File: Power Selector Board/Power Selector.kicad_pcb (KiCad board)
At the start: 2 copper layers, 23 parts, among them J101 MSD-DB01M-12P, J102 MSD-DB01F-12P_1, J103 64900221122, J104 64900221122, J105 64900221122, K101 G6SK-2G DC24, K102 J115F11C24VDCSH.9, K103 J115F11C24VDCSH.9, U101 1720466, U102 LMW78_24-0.3RL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

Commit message: Debut routing
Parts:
- removed K102, K103: J115F11C24VDCSH.9, Relays:RELAY5_J115F11C24VDCSH.9_CRS
- added H1: Mounting-Hole-M3, Connectors:Mounting_Hole_3mm, F.Cu at (58.2, 81.8)
- added H2: Mounting-Hole-M3, Connectors:Mounting_Hole_3mm, F.Cu at (58.2, 87.8)
- added H3: Mounting-Hole-M3, Connectors:Mounting_Hole_3mm, F.Cu at (58.2, 93.8)
- added H4: Mounting-Hole-M3, Connectors:Mounting_Hole_3mm, F.Cu at (58.2, 99.8)
- added RL101: RELAY8_SMTGUL_TEC, Relays:2-1462039-9, F.Cu at (166.8, 82.8)
- J101, J102: footprint Connectors:649012227222 -> Connectors:MSD-DB01F-12P-V2.0
- moved J101 107.0 mm to (206.0, 77.0), turned to -90 degrees
- moved F102 98.2 mm to (192.1, 82.6)
- moved F103 82.5 mm to (81.8, 83.7)
- moved J104 58.8 mm to (100.2, 67.3)
- moved J103 58.5 mm to (93.8, 67.5)
- moved F101 57.6 mm to (149.0, 119.4), turned to 180 degrees
- moved D101 55.4 mm to (129.3, 67.4)
- moved D102 55.4 mm to (129.3, 71.7)
- moved D103 55.4 mm to (129.3, 76.1)
- moved U101 50.3 mm to (145.2, 127.1)
- moved R101 49.5 mm to (112.8, 125.8), turned to 180 degrees
- moved J105 48.2 mm to (108.4, 130.8), turned to -90 degrees
- moved U102 43.3 mm to (96.4, 86.9), turned to 90 degrees
- moved C103 34.9 mm to (142.8, 107.0), turned to 90 degrees
- moved C102 34.4 mm to (142.8, 97.7), turned to -90 degrees
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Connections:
- C103 pad 2: 24V_Bat -> 24V
- C104 pad 2: 24V_Tether -> 24V
- F101 pad 1: +V_Drone -> (no net)
- F101 pad 2: Net-(F101-Pad2) -> (no net)
- F102 pad 1: +V_Bat -> (no net)
- F102 pad 2: Net-(F102-Pad2) -> (no net)
- F103 pad 1: +V_Bat -> +VBat
- F104 pad 1: +V_Drone -> +VBat
- J101 pad 1: +V_Drone -> Net-(F102-Pad~)
- J101 pad 2: +V_Drone -> Net-(F102-Pad~)
- J101 pad 3: +V_Drone -> Net-(F102-Pad~)
- J101 pad 4: +V_Drone -> Net-(F102-Pad~)
- J101 pad 5: +V_Drone -> Net-(F102-Pad~)
- J102 pad 1: Net-(F102-Pad2) -> +VBat
- J102 pad 2: Net-(F102-Pad2) -> +VBat
- J102 pad 3: Net-(F102-Pad2) -> +VBat
- J102 pad 4: Net-(F102-Pad2) -> +VBat
- J102 pad 5: Net-(F102-Pad2) -> +VBat
- J103 pad 1: 24V_Tether -> 24V
- J103 pad 2: Net-(D103-Pad1) -> Net-(J103-Pad2)
- J104 pad 1: Net-(J104-Pad1) -> GND
- J104 pad 2: GND -> Net-(J104-Pad2)
- J105 pad 1: 24V_Bat -> 24V
- K101 pad 1: Net-(D103-Pad1) -> GND
- K101 pad 12: GND -> Net-(J103-Pad2)
- K101 pad 6: 24V_Bat -> 24V
- K101 pad 8: 24V_Tether -> 24V
- K101 pad 9: /Relay_Active -> Net-(K101-Pad9)
- U101 pad 1: Net-(F101-Pad2) -> Net-(F101-Pad~)
- U101 pad 2: Net-(F101-Pad2) -> Net-(F101-Pad~)
- U101 pad 3: Net-(F101-Pad2) -> Net-(F101-Pad~)
- U102 pad 3: 24V_Bat -> 24V
- U103 pad 3: 24V_Tether -> 24V
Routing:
- net 24V: track 0.00 -> 62.9 mm
- net +VBat: track 0.00 -> 37.3 mm
- net Net-(U102-Vin): track 0.00 -> 14.5 mm
- net Net-(U103-Vin): track 0.00 -> 13.2 mm
- net Net-(J105-Pad2): track 0.00 -> 5.62 mm
- net (no net): track 0.00 -> 4.20 mm
- added copper zone on F.Cu, net +VBat
- added copper zone on B.Cu, net GND
- added copper zone on F.Cu, net GND
- added copper zone on F.Cu, net Net-(F101-Pad~)
- added copper zone on F.Cu, net Net-(F102-Pad~)
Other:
- board text added: "DOIT ETRE PLACÉ AU CENTRE EN X ET EN BAS EN Y POUR AVOIR UN FIT IDENTIQUE DE CHAQUE CÔTÉ DU DRONE"

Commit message: Fix du bug github, devrait etre la bonne version
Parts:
- removed H1, H2, H3, H4: Mounting-Hole-M3, Connectors:Mounting_Hole_3mm
- removed RL101: RELAY8_SMTGUL_TEC, Relays:2-1462039-9
- added K102: J115F11C24VDCSH.9, Relays:RELAY5_J115F11C24VDCSH.9_CRS, F.Cu at (120.1, 77.9)
- added K103: J115F11C24VDCSH.9, Relays:RELAY5_J115F11C24VDCSH.9_CRS, F.Cu at (149.8, 77.9)
- J101, J102: footprint Connectors:MSD-DB01F-12P-V2.0 -> Connectors:649012227222
- moved J101 107.0 mm to (100.1, 61.8), turned to 0 degrees
- moved F102 98.2 mm to (96.8, 106.4)
- moved F103 82.5 mm to (162.7, 99.8)
- moved J104 58.8 mm to (143.6, 107.0)
- moved J103 58.5 mm to (136.9, 107.0)
- moved F101 57.6 mm to (96.7, 95.2), turned to 0 degrees
- moved D101 55.4 mm to (182.5, 82.7)
- moved D102 55.4 mm to (182.5, 87.0)
- moved D103 55.4 mm to (182.5, 91.3)
- moved U101 50.3 mm to (119.9, 83.6)
- moved R101 49.5 mm to (159.1, 108.5), turned to 0 degrees
- moved J105 48.2 mm to (150.3, 107.0), turned to 0 degrees
- moved U102 43.3 mm to (139.6, 84.7), turned to 0 degrees
- moved C103 34.9 mm to (108.5, 101.0), turned to 0 degrees
- moved C102 34.4 mm to (108.5, 96.7), turned to 0 degrees
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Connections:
- C103 pad 2: 24V -> 24V_Bat
- C104 pad 2: 24V -> 24V_Tether
- F101 pad 1: (no net) -> +V_Drone
- F101 pad 2: (no net) -> Net-(F101-Pad2)
- F102 pad 1: (no net) -> +V_Bat
- F102 pad 2: (no net) -> Net-(F102-Pad2)
- F103 pad 1: +VBat -> +V_Bat
- F104 pad 1: +VBat -> +V_Drone
- J101 pad 1: Net-(F102-Pad~) -> +V_Drone
- J101 pad 2: Net-(F102-Pad~) -> +V_Drone
- J101 pad 3: Net-(F102-Pad~) -> +V_Drone
- J101 pad 4: Net-(F102-Pad~) -> +V_Drone
- J101 pad 5: Net-(F102-Pad~) -> +V_Drone
- J102 pad 1: +VBat -> Net-(F102-Pad2)
- J102 pad 2: +VBat -> Net-(F102-Pad2)
- J102 pad 3: +VBat -> Net-(F102-Pad2)
- J102 pad 4: +VBat -> Net-(F102-Pad2)
- J102 pad 5: +VBat -> Net-(F102-Pad2)
- J103 pad 1: 24V -> 24V_Tether
- J103 pad 2: Net-(J103-Pad2) -> Net-(D103-Pad1)
- J104 pad 1: GND -> Net-(J104-Pad1)
- J104 pad 2: Net-(J104-Pad2) -> GND
- J105 pad 1: 24V -> 24V_Bat
- K101 pad 1: GND -> Net-(D103-Pad1)
- K101 pad 12: Net-(J103-Pad2) -> GND
- K101 pad 6: 24V -> 24V_Bat
- K101 pad 8: 24V -> 24V_Tether
- K101 pad 9: Net-(K101-Pad9) -> /Relay_Active
- U101 pad 1: Net-(F101-Pad~) -> Net-(F101-Pad2)
- U101 pad 2: Net-(F101-Pad~) -> Net-(F101-Pad2)
- U101 pad 3: Net-(F101-Pad~) -> Net-(F101-Pad2)
- U102 pad 3: 24V -> 24V_Bat
- U103 pad 3: 24V -> 24V_Tether
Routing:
- net 24V: track 62.9 -> 0.00 mm
- net +VBat: track 37.3 -> 0.00 mm
- net Net-(U102-Vin): track 14.5 -> 0.00 mm
- net Net-(U103-Vin): track 13.2 -> 0.00 mm
- net Net-(J105-Pad2): track 5.62 -> 0.00 mm
- net (no net): track 4.20 -> 0.00 mm
- removed copper zone on F.Cu, net +VBat
- removed copper zone on B.Cu, net GND
- removed copper zone on F.Cu, net GND
- removed copper zone on F.Cu, net Net-(F101-Pad~)
- removed copper zone on F.Cu, net Net-(F102-Pad~)
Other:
- board text removed: "DOIT ETRE PLACÉ AU CENTRE EN X ET EN BAS EN Y POUR AVOIR UN FIT IDENTIQUE DE CHAQUE CÔTÉ DU DRONE"

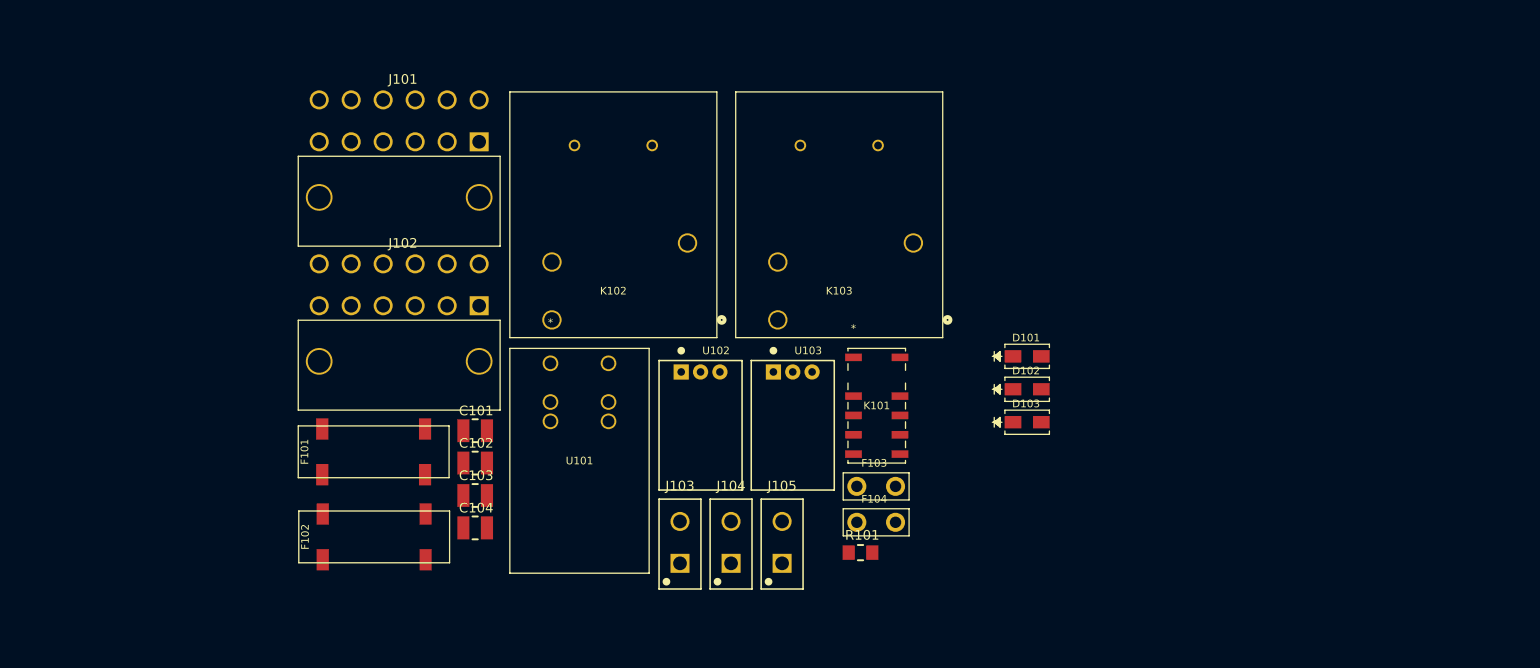
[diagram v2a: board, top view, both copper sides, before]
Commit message: Ajout des deux PCB (droit et gauche) sur le meme PCB
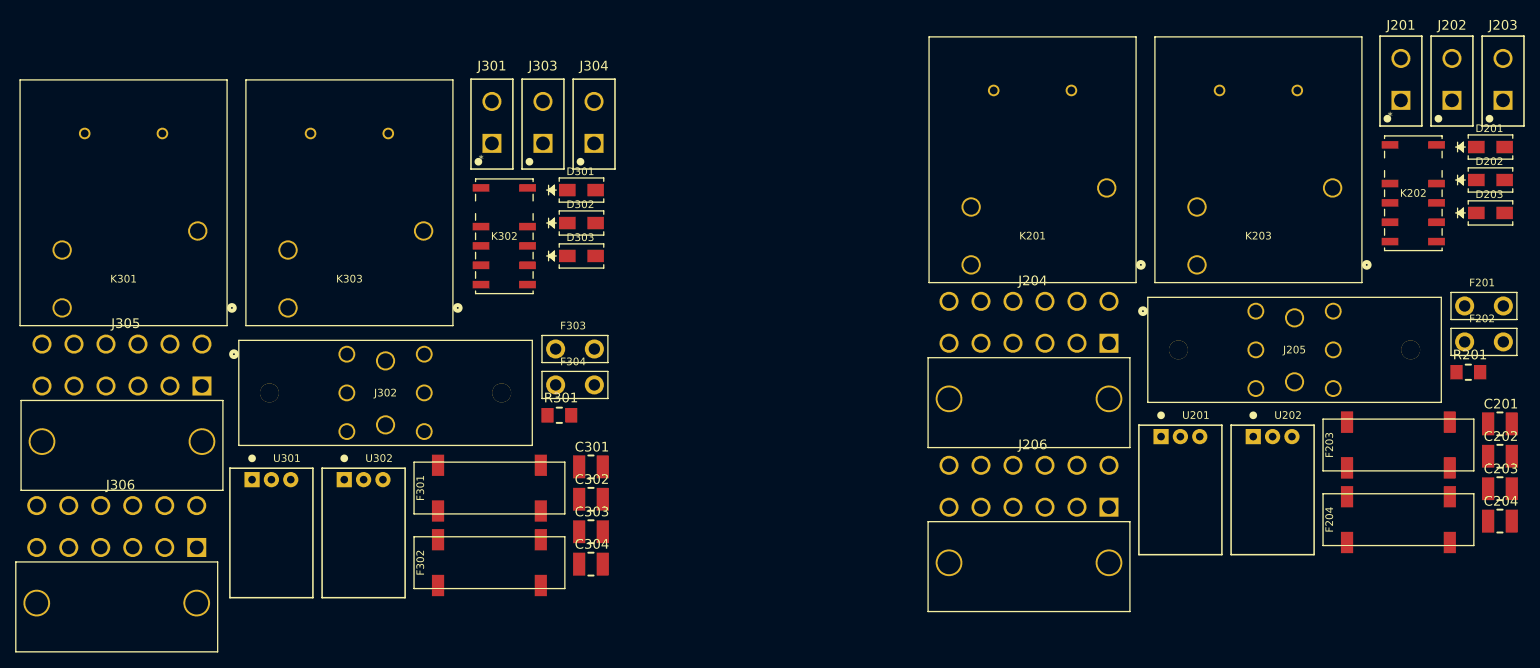
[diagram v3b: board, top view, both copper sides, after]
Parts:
- removed C101, C102, C103, C104: GRM32EC72A106ME05L, Capacitors:C1210
- removed D101, D102, D103: S1D-13-F, Diodes:SMA_DIO
- removed F101, F102: 047706.3MRET1P, Fuses:3587TR
- removed F103, F104: 0698Q2000-02, Fuses:TE5_395
- removed J101: MSD-DB01M-12P, Connectors:649012227222
- removed J102: MSD-DB01F-12P_1, Connectors:649012227222
- removed J103, J104, J105: 64900221122, Connectors:64900221122
- removed K101: G6SK-2G DC24, Relays:G6SK-2G DC3_OMR
- removed K102, K103: J115F11C24VDCSH.9, Relays:RELAY5_J115F11C24VDCSH.9_CRS
- removed R101: RC1206JR-07120RL, Resistors:R1206
- removed U101: 1720466, Connectors:1720466_PXC
- removed U102, U103: LMW78_24-0.3RL, Assembly:OKI-78SR_Horizontal
- added C201: GRM32EC72A106ME05L, Capacitors:C1210, F.Cu at (243.0, 91.6)
- added C202: GRM32EC72A106ME05L, Capacitors:C1210, F.Cu at (243.0, 95.8)
- added C203: GRM32EC72A106ME05L, Capacitors:C1210, F.Cu at (243.0, 100.1)
- added C204: GRM32EC72A106ME05L, Capacitors:C1210, F.Cu at (243.0, 104.3)
- added C301: GRM32EC72A106ME05L, Capacitors:C1210, F.Cu at (123.7, 97.2)
- added C302: GRM32EC72A106ME05L, Capacitors:C1210, F.Cu at (123.7, 101.5)
- added C303: GRM32EC72A106ME05L, Capacitors:C1210, F.Cu at (123.7, 105.7)
- added C304: GRM32EC72A106ME05L, Capacitors:C1210, F.Cu at (123.7, 110.0)
- added D201: S1D-13-F, Diodes:SMA_DIO, F.Cu at (243.3, 55.2)
- added D202: S1D-13-F, Diodes:SMA_DIO, F.Cu at (243.3, 59.5)
- added D203: S1D-13-F, Diodes:SMA_DIO, F.Cu at (243.3, 63.9)
- added D301: S1D-13-F, Diodes:SMA_DIO, F.Cu at (124.0, 60.9)
- added D302: S1D-13-F, Diodes:SMA_DIO, F.Cu at (124.0, 65.2)
- added D303: S1D-13-F, Diodes:SMA_DIO, F.Cu at (124.0, 69.5)
- added F201: 0698Q2000-02, Fuses:TE5_395, F.Cu at (242.5, 76.1)
- added F202: 0698Q2000-02, Fuses:TE5_395, F.Cu at (242.5, 80.8)
- added F203: 047706.3MRET1P, Fuses:3587TR, F.Cu at (231.2, 94.3)
- added F204: 047706.3MRET1P, Fuses:3587TR, F.Cu at (231.2, 104.1)
- added F301: 047706.3MRET1P, Fuses:3587TR, F.Cu at (111.9, 100.0)
- added F302: 047706.3MRET1P, Fuses:3587TR, F.Cu at (111.9, 109.8)
- added F303: 0698Q2000-02, Fuses:TE5_395, F.Cu at (123.1, 81.7)
- added F304: 0698Q2000-02, Fuses:TE5_395, F.Cu at (123.1, 86.4)
- added J201: 64900221122, Connectors:64900221122, F.Cu at (231.6, 46.2)
- added J202: 64900221122, Connectors:64900221122, F.Cu at (238.3, 46.2)
- added J203: 64900221122, Connectors:64900221122, F.Cu at (245.0, 46.2)
- added J204: MSD-DB01M-12P, Connectors:649012227222, F.Cu at (182.7, 88.3)
- added J205: 1998865, Connectors:1998865, F.Cu at (212.5, 76.8)
- added J206: MSD-DB01F-12P_1, Connectors:649012227222, F.Cu at (182.7, 109.8)
- added J301: 64900221122, Connectors:64900221122, F.Cu at (112.2, 51.9)
- added J302: 1998865, Connectors:1998865, F.Cu at (93.2, 82.4)
- added J303: 64900221122, Connectors:64900221122, F.Cu at (118.9, 51.9)
- added J304: 64900221122, Connectors:64900221122, F.Cu at (125.6, 51.9)
- added J305: MSD-DB01M-12P, Connectors:649012227222, F.Cu at (63.7, 93.9)
- added J306: MSD-DB01F-12P_1, Connectors:649012227222, F.Cu at (63.0, 115.1)
- added K201: J115F11C24VDCSH.9, Relays:RELAY5_J115F11C24VDCSH.9_CRS, F.Cu at (175.1, 70.7)
- added K202: G6SK-2G DC24, Relays:G6SK-2G DC3_OMR, F.Cu at (233.2, 61.3)
- added K203: J115F11C24VDCSH.9, Relays:RELAY5_J115F11C24VDCSH.9_CRS, F.Cu at (204.8, 70.7)
- added K301: J115F11C24VDCSH.9, Relays:RELAY5_J115F11C24VDCSH.9_CRS, F.Cu at (55.8, 76.3)
- added K302: G6SK-2G DC24, Relays:G6SK-2G DC3_OMR, F.Cu at (113.9, 66.9)
- added K303: J115F11C24VDCSH.9, Relays:RELAY5_J115F11C24VDCSH.9_CRS, F.Cu at (85.5, 76.3)
- added R201: RC1206JR-07120RL, Resistors:R1206, F.Cu at (238.9, 84.8)
- added R301: RC1206JR-07120RL, Resistors:R1206, F.Cu at (119.5, 90.4)
- added U201: LMW78_24-0.3RL, Assembly:OKI-78SR_Horizontal, F.Cu at (202.6, 93.2)
- added U202: LMW78_24-0.3RL, Assembly:OKI-78SR_Horizontal, F.Cu at (214.7, 93.2)
- added U301: LMW78_24-0.3RL, Assembly:OKI-78SR_Horizontal, F.Cu at (83.3, 98.9)
- added U302: LMW78_24-0.3RL, Assembly:OKI-78SR_Horizontal, F.Cu at (95.4, 98.9)

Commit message: Premier commit pour routing PCB. Modif footprint connecteur batterie.
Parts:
- added H1: Mounting-Hole-M3, Connectors:Mounting_Hole_3mm, F.Cu at (141.0, 51.4)
- added H2: Mounting-Hole-M3, Connectors:Mounting_Hole_3mm, F.Cu at (141.0, 57.4)
- added H3: Mounting-Hole-M3, Connectors:Mounting_Hole_3mm, F.Cu at (141.0, 63.4)
- added H4: Mounting-Hole-M3, Connectors:Mounting_Hole_3mm, F.Cu at (141.0, 69.4)
- added H5: Mounting-Hole-M3, Connectors:Mounting_Hole_3mm, F.Cu at (164.0, 70.4)
- added H6: Mounting-Hole-M3, Connectors:Mounting_Hole_3mm, F.Cu at (268.6, 71.0)
- added H7: Mounting-Hole-M3, Connectors:Mounting_Hole_3mm, F.Cu at (269.2, 128.4)
- added H8: Mounting-Hole-M3, Connectors:Mounting_Hole_3mm, F.Cu at (164.4, 128.0)
- J204, J206, J305, J306: footprint Connectors:649012227222 -> Connectors:MSD-DB01F-12P-V2.0
- moved J305 208.6 mm to (272.0, 84.4), turned to -90 degrees
- moved K301 181.5 mm to (234.4, 108.6), turned to -90 degrees
- moved J204 161.5 mm to (21.6, 99.0)
- moved J206 161.2 mm to (21.6, 106.8)
- moved K303 149.1 mm to (234.5, 73.2), turned to -90 degrees
- moved C201 141.2 mm to (103.3, 111.7)
- moved C202 141.2 mm to (103.3, 115.9)
- moved C203 141.2 mm to (103.3, 120.2)
- moved C204 141.2 mm to (103.3, 124.4)
- moved D201 141.2 mm to (103.6, 75.3)
- moved D202 141.2 mm to (103.6, 79.7)
- moved D203 141.2 mm to (103.6, 84.0)
- moved F201 141.2 mm to (102.7, 96.2)
- moved F202 141.2 mm to (102.7, 100.9)
- moved F203 141.2 mm to (91.5, 114.4)
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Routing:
- net 24V_Bat_D: track 0.00 -> 129.0 mm, vias 0 -> 2
- net /PCB_Droit/Relay_Active: track 0.00 -> 118.1 mm
- net Vin_Bat_D: track 0.00 -> 98.7 mm
- net Net-(J303-Pad1): track 0.00 -> 75.0 mm, vias 0 -> 1
- net +Vin_Tether_D: track 0.00 -> 69.6 mm
- net Net-(K301-Pad1): track 0.00 -> 67.5 mm
- net 24V_Tether_D: track 0.00 -> 63.3 mm
- net Net-(D301-Pad1): track 0.00 -> 37.9 mm
- net Net-(U301-Vin): track 0.00 -> 21.9 mm
- net Net-(F301-Pad2): track 0.00 -> 20.1 mm
- net Net-(U302-Vin): track 0.00 -> 18.1 mm
- net Net-(J301-Pad2): track 0.00 -> 6.74 mm
- net +Vin_Drone_D: track 0.00 -> 1.00 mm
- added copper zone on F.Cu, net +Vin_Drone_D
- added copper zone on B.Cu, net GND_D
- added copper zone on F.Cu, net GND_D
- added copper zone on B.Cu, net GND_G
- added copper zone on F.Cu, net GND_G
- added copper zone on F.Cu, net Net-(F302-Pad2)
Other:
- board outline added: 113.9 x 67.2 mm

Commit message: Routing PCB gauche. Prêt pour review 1.
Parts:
- moved J204 118.9 mm to (139.7, 85.8), turned to -90 degrees
- moved H4 96.8 mm to (65.7, 130.2)
- moved H3 75.6 mm to (65.7, 70.2)
- moved H2 73.0 mm to (135.7, 130.2)
- moved K201 66.3 mm to (97.9, 113.0), turned to -90 degrees
- moved D203 46.2 mm to (135.0, 117.8), turned to -90 degrees
- moved J206 45.8 mm to (62.1, 85.4), turned to -90 degrees
- moved J203 43.1 mm to (131.8, 100.3)
- moved J202 43.1 mm to (125.1, 100.3)
- moved K203 42.8 mm to (102.7, 70.4), turned to -90 degrees
- moved F204 41.4 mm to (69.1, 89.4), turned to -90 degrees
- moved F201 39.6 mm to (72.3, 70.8), turned to 90 degrees
- moved C202 39.0 mm to (76.9, 87.2)
- moved U201 36.6 mm to (81.7, 82.0), turned to 180 degrees
- moved J201 36.1 mm to (77.8, 99.6), turned to 180 degrees
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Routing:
- net 24V_Tether_G: track 0.00 -> 108.6 mm, vias 0 -> 3
- net /PCB_Gauche/Relay_Active: track 0.00 -> 93.7 mm, vias 0 -> 4
- net /PCB_Gauche/SDA: track 0.00 -> 87.3 mm, vias 0 -> 2
- net /PCB_Gauche/SCL: track 0.00 -> 86.7 mm, vias 0 -> 2
- net +Vin_Tether_G: track 0.00 -> 82.8 mm
- net Net-(D201-Pad1): track 0.00 -> 60.8 mm, vias 0 -> 2
- net Net-(K201-Pad1): track 0.00 -> 59.1 mm, vias 0 -> 1
- net Vin_Bat_G: track 0.00 -> 46.2 mm
- net Net-(J202-Pad1): track 0.00 -> 42.2 mm, vias 0 -> 1
- net 24V_Bat_G: track 0.00 -> 28.8 mm, vias 0 -> 2
- net Net-(U202-Vin): track 0.00 -> 26.1 mm
- net Net-(U201-Vin): track 0.00 -> 25.9 mm
- net Net-(F203-Pad2): track 0.00 -> 24.6 mm
- net Net-(J201-Pad2): track 0.00 -> 6.09 mm
- net +Vin_Drone_G: track 0.00 -> 2.62 mm, vias 0 -> 14
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- added copper zone on B.Cu, net +Vin_Drone_G
- added copper zone on F.Cu, net +Vin_Drone_G
- added copper zone on F.Cu, net Net-(F204-Pad2)
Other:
- board size 113.9 x 67.2 mm -> 213 x 70.8 mm

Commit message: Ajout testpoints au schéma et PCB. Ajout de commentaires sur le silkscreen.
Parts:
- added TP1: Vin Bat, Connectors:Keystone_5001, F.Cu at (136.6, 125.5)
- added TP2: 24V Bat, Connectors:Keystone_5001, F.Cu at (136.4, 119.0)
- added TP3: Vin Tether, Connectors:Keystone_5001, F.Cu at (131.2, 125.3)
- added TP4: 24V Tether, Connectors:Keystone_5001, F.Cu at (131.2, 118.8)
- added TP5: GND, Connectors:Keystone_5001, F.Cu at (133.3, 113.4)
- added TP6: Vout Drone, Connectors:Keystone_5001, F.Cu at (131.2, 131.9)
- moved D203 9.41 mm to (134.6, 108.4), turned to 0 degrees
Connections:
- J202 pad 1: Net-(J202-Pad1) -> +Vin_Tether_G
- K201 pad 3: Net-(J202-Pad1) -> +Vin_Tether_G
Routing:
- net Vin_Bat_G: track 46.2 -> 172.6 mm
- net 24V_Bat_G: track 28.8 -> 125.4 mm, vias 2 -> 3
- net +Vin_Tether_G: track 82.8 -> 144.7 mm, vias 0 -> 1
- net +Vin_Drone_G: track 2.62 -> 50.1 mm
- net Net-(J202-Pad1): track 42.2 -> 0.00 mm, vias 1 -> 0
- net 24V_Tether_G: track 108.6 -> 111.5 mm
- net Net-(U202-Vin): track 26.1 -> 24.8 mm
- net /PCB_Gauche/Relay_Active: track 93.7 -> 94.7 mm
- net GND_G: vias 57 -> 54
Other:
- board text added: "24V Bat"
- board text added: "24V Tet"
- board text added: "Bat IN"
- board text added: "Drone OUT"
- board text added: "GND"
- board text added: "LED"
- board text added: "NC"
- board text added: "NO"
- board text added: "PFE ÉTS E2023 - Pour WINDO Contrôle d'alimentation pour drone Schéma électrique : Kevin Lalonde Design PCB : Tristan Legault Review : Guyaume Morand"
- board text added: "Vin Bat"
- board text added: "Vin Tet"
- board text added: "Vout"
